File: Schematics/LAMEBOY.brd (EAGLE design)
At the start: 45.7 x 67.3 mm, 65 parts, among them IC1 PCF8574T, IC3 MCP73831, Q1 12MHz, U1 USD-SOCKETMICROSDEBAY, U2 USB

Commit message: labelstuff
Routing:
- net VCC: track 261.0 -> 260.4 mm
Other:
- board text added: "This will come in handy one day"
- board text removed: "This will come in handy one day. Please help."
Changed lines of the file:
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@@
 <wire x1="29.21" y1="28.448" x2="29.21" y2="14.732" width="0.254" layer="25"/>
 <wire x1="29.21" y1="14.732" x2="45.339" y2="14.732" width="0.254" layer="25"/>
-<text x="38.608" y="28.702" size="1.778" layer="25" ratio="12">SD</text>
+<text x="41.402" y="28.702" size="1.778" layer="25" ratio="12" rot="R90">SD</text>
 <text x="0.508" y="56.642" size="1.778" layer="26" ratio="15" rot="MR90">RST</text>
 <text x="45.085" y="58.039" size="1.778" layer="26" ratio="15" rot="MR0">C</text>
@@
 serial
 converter</text>
-<text x="38.1" y="21.59" size="1.016" layer="25" ratio="12" distance="5" rot="R180" align="center">This will come in
-handy one day.
-Please help.</text>
+<text x="38.1" y="21.59" size="1.016" layer="25" ratio="12" distance="5" rot="R180" align="center">This will come
+in handy
+one day</text>
 </plain>
 <attributes>
@@
 <contactref element="S2" pad="1"/>
 <wire x1="40.005" y1="52.07" x2="40.767" y2="51.308" width="0.4064" layer="1"/>
-<wire x1="40.767" y1="51.308" x2="40.767" y2="31.75" width="0.4064" layer="1"/>
-<wire x1="26.86091875" y1="31.2592" x2="40.2762" y2="31.2592" width="0.4064" layer="16"/>
-<wire x1="40.2762" y1="31.2592" x2="40.767" y2="31.75" width="0.4064" layer="16"/>
-<via x="40.767" y="31.75" extent="1-16" drill="0.3302" diameter="1.016"/>
+<wire x1="40.767" y1="51.308" x2="40.767" y2="32.512" width="0.4064" layer="1"/>
+<wire x1="26.86091875" y1="31.2592" x2="39.5142" y2="31.2592" width="0.4064" layer="16"/>
+<wire x1="39.5142" y1="31.2592" x2="40.767" y2="32.512" width="0.4064" layer="16"/>
+<via x="40.767" y="32.512" extent="1-16" drill="0.3302" diameter="1.016"/>
 <wire x1="21.86091875" y1="31.2592" x2="21.86091875" y2="34.90808125" width="0.4064" layer="16"/>
 <wire x1="21.86091875" y1="34.90808125" x2="21.844" y2="35.052" width="0.4064" layer="16"/>
@@
 <contactref element="C3" pad="P$1"/>
 <wire x1="34.326" y1="63.782" x2="34.326" y2="62.194" width="0.254" layer="1"/>
-<wire x1="40.64" y1="31.623" x2="40.767" y2="31.75" width="0.4064" layer="1"/>
 <contactref element="U$10" pad="P$2"/>
 <wire x1="2.286" y1="25.13" x2="2.27" y2="25.146" width="0.4064" layer="1"/>

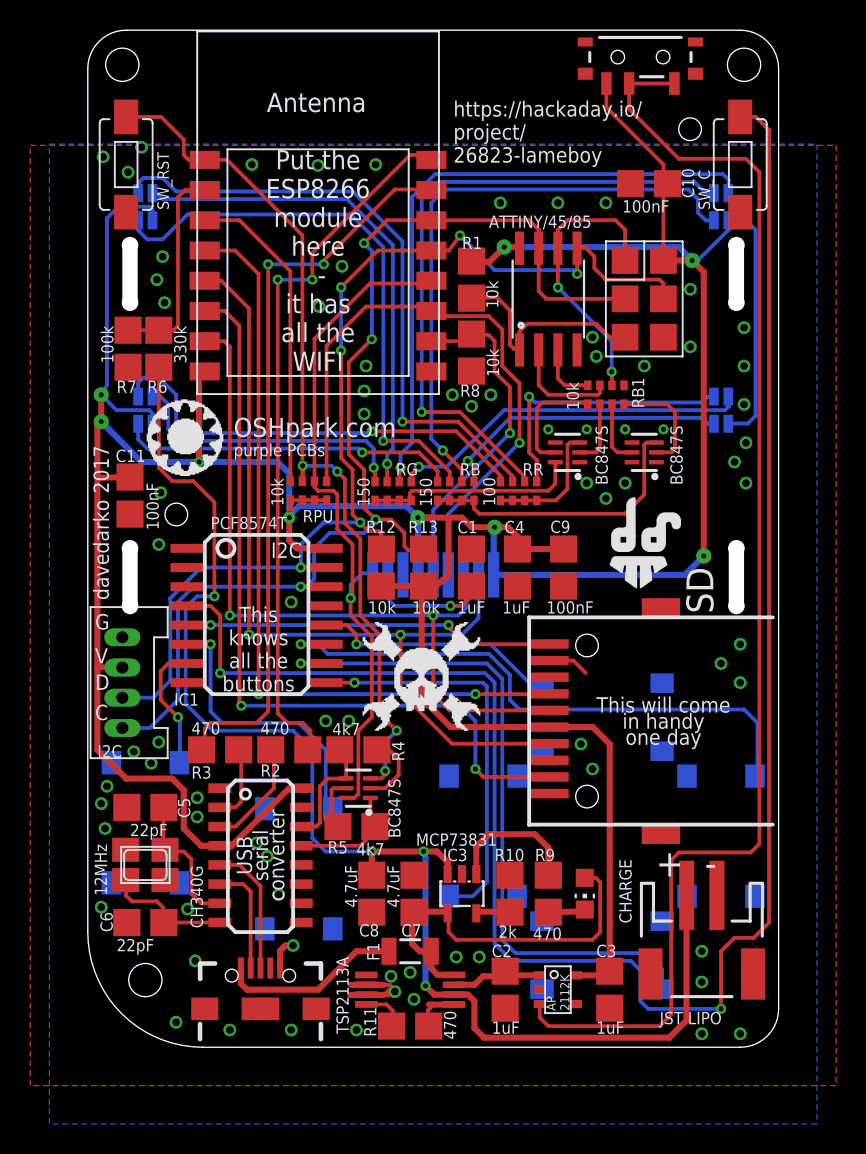
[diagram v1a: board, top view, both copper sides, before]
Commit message: moved C and RST switch
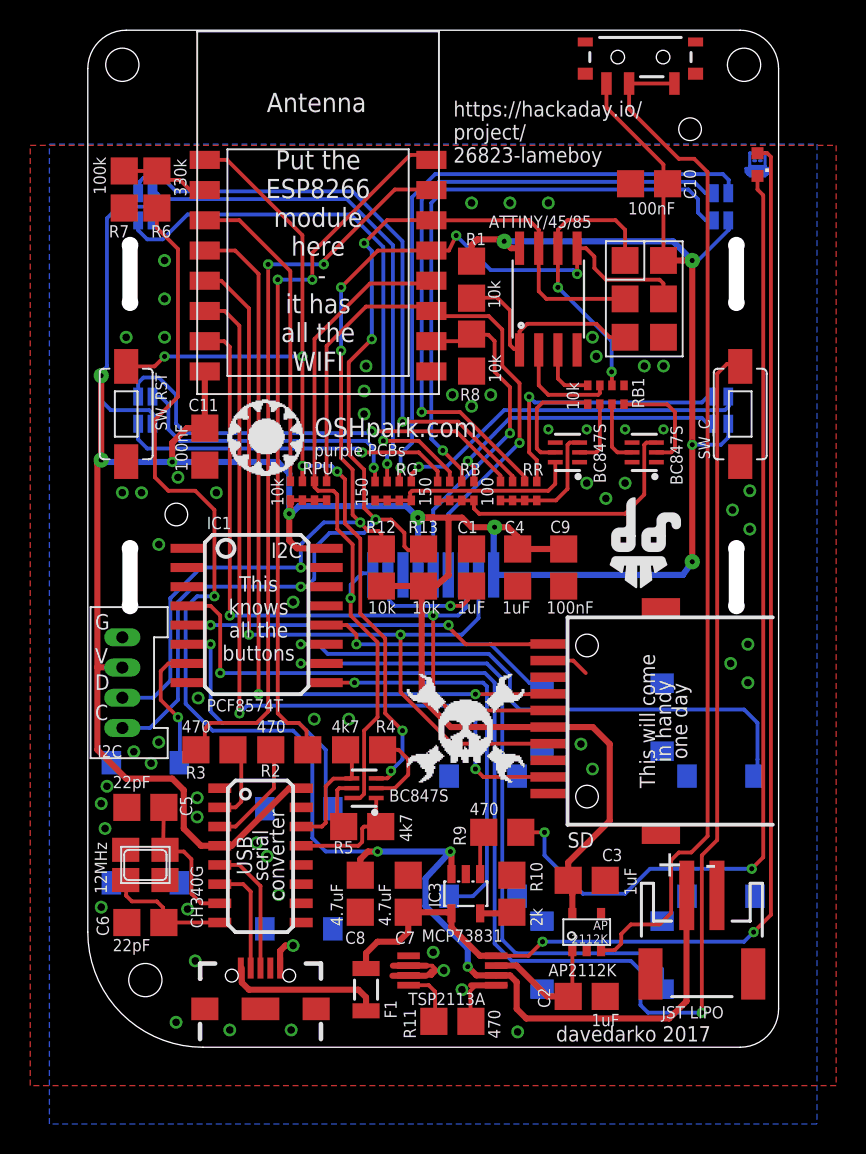
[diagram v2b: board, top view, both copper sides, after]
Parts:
- removed U$8: (no value), LOGOS:DAVEDARKO_GOLD
- added U$13: (no value), LOGOS:DAVEDARKO_GOLD
- CHARGE: device led:CHIP-LED0805 -> led:CHIPLED_0603_CHARLIE
- moved CHARGE 49.6 mm to (44.3, 58.4)
- moved SW_C 16.5 mm to (43.2, 41.9)
- moved SW_RST 16.5 mm to (2.54, 41.9)
- moved R7 10.5 mm to (2.41, 56.8)
- moved R6 10.5 mm to (4.57, 56.8)
- moved C3 7.40 mm to (33.0, 11.0), turned to 0 degrees
- moved C11 5.92 mm to (7.75, 39.8)
- moved C2 5.42 mm to (33.0, 3.37), turned to 0 degrees
- moved U$5 5.33 mm to (20.7, 40.4)
- moved R9 5.08 mm to (27.4, 14.2), turned to 180 degrees
- moved U$12 4.50 mm to (25.0, 20.8)
- moved U$9 4.26 mm to (33.0, 7.62), turned to 180 degrees
- moved F1 3.87 mm to (18.4, 3.81), turned to 90 degrees
- moved U$4 3.07 mm to (24.1, 5.08)
- moved R11 2.81 mm to (24.1, 1.71)
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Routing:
- net N$15: track 2.47 -> 64.9 mm, vias 0 -> 2
- net VBUS: track 24.9 -> 83.7 mm, vias 0 -> 2
- net BTN_C: track 122.4 -> 103.5 mm
- net VCC: track 260.4 -> 242.3 mm, vias 9 -> 10
- net VREG_EN: track 86.1 -> 68.2 mm
- net VBAT: track 94.4 -> 103.4 mm
- net ADC: track 14.4 -> 5.85 mm
- net N$12: track 9.11 -> 2.82 mm
- net N$16: track 0.00 -> 5.33 mm
- net RST_ESP: track 58.4 -> 63.5 mm, vias 4 -> 6
- net N$1: track 0.00 -> 3.81 mm
- net N$14: track 0.00 -> 2.03 mm
- net VREG_IN: track 6.76 -> 8.75 mm
- net N$20: track 3.17 -> 4.73 mm
- net VUSB: track 12.0 -> 10.5 mm
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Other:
- board text added: "AP2112K"
- board text added: "USB"

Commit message: usb logo
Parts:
- moved U$13 0.13 mm to (34.0, 12.8)
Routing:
- net N$14: track 2.03 -> 8.08 mm
- net N$16: track 5.33 -> 0.00 mm
- net N$15: track 64.9 -> 65.7 mm
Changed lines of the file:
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@@
 <layer number="28" name="bValues" color="7" fill="1" visible="no" active="yes"/>
 <layer number="29" name="tStop" color="7" fill="3" visible="no" active="yes"/>
-<layer number="30" name="bStop" color="7" fill="6" visible="yes" active="yes"/>
+<layer number="30" name="bStop" color="7" fill="6" visible="no" active="yes"/>
 <layer number="31" name="tCream" color="7" fill="4" visible="no" active="yes"/>
 <layer number="32" name="bCream" color="7" fill="5" visible="no" active="yes"/>
@@
 <element name="U$11" library="LOGOS" package="DAVEDARKO2_LOGO" value="" x="36.449" y="32.639"/>
 <element name="U$12" library="LOGOS" package="HACKADAY_LOGO" value="" x="24.9555" y="20.7645"/>
-<element name="U$13" library="LOGOS" package="DAVEDARKO_GOLD" value="" x="34.036" y="12.954" rot="MR0"/>
+<element name="U$13" library="LOGOS" package="DAVEDARKO_GOLD" value="" x="34.036" y="12.827" rot="MR0"/>
 </elements>
 <signals>
@@
 <via x="43.942" y="11.811" extent="1-16" drill="0.3302"/>
 <wire x1="28.657" y1="14.224" x2="30.226" y2="14.224" width="0.254" layer="1"/>
-<wire x1="30.226" y1="14.224" x2="30.226" y2="12.7" width="0.254" layer="16"/>
-<wire x1="30.226" y1="12.7" x2="32.766" y2="10.16" width="0.254" layer="16"/>
-<wire x1="32.766" y1="10.16" x2="35.56" y2="10.16" width="0.254" layer="16"/>
-<wire x1="35.56" y1="10.16" x2="37.211" y2="11.811" width="0.254" layer="16"/>
-<wire x1="37.211" y1="11.811" x2="43.942" y2="11.811" width="0.254" layer="16"/>
+<wire x1="30.226" y1="14.224" x2="30.226" y2="11.43" width="0.254" layer="16"/>
+<wire x1="30.226" y1="11.43" x2="31.75" y2="10.033" width="0.254" layer="16"/>
+<wire x1="31.75" y1="10.033" x2="35.56" y2="10.033" width="0.254" layer="16"/>
+<wire x1="35.56" y1="10.033" x2="37.338" y2="11.811" width="0.254" layer="16"/>
+<wire x1="37.338" y1="11.811" x2="43.942" y2="11.811" width="0.254" layer="16"/>
 <via x="30.226" y="14.224" extent="1-16" drill="0.3302"/>
 </signal>
@@
 </signal>
 <signal name="N$1">
-<wire x1="43.815" y1="59.182" x2="44.831" y2="59.182" width="0.2032" layer="16"/>
-<wire x1="44.831" y1="59.182" x2="44.831" y2="58.293" width="0.2032" layer="16"/>
+<wire x1="43.942" y1="59.182" x2="44.704" y2="59.182" width="0.2032" layer="16"/>
+<wire x1="44.704" y1="59.182" x2="44.831" y2="59.055" width="0.2032" layer="16"/>
+<wire x1="44.831" y1="59.055" x2="44.831" y2="58.293" width="0.2032" layer="16"/>
 <wire x1="44.831" y1="58.293" x2="43.815" y2="58.293" width="0.2032" layer="16"/>
-<wire x1="43.815" y1="58.293" x2="43.815" y2="59.182" width="0.2032" layer="16"/>
+<wire x1="43.815" y1="58.293" x2="43.815" y2="59.055" width="0.2032" layer="16"/>
+<wire x1="43.815" y1="59.055" x2="43.942" y2="59.182" width="0.2032" layer="16"/>
 </signal>
 <signal name="N$2">
@@
 <wire x1="43.561" y1="58.166" x2="45.085" y2="58.166" width="0.2032" layer="16"/>
 <wire x1="45.085" y1="58.166" x2="45.085" y2="57.912" width="0.2032" layer="16"/>
-</signal>
-<signal name="N$16">
 <wire x1="43.688" y1="58.039" x2="44.958" y2="58.039" width="0.2032" layer="16"/>
 <wire x1="44.958" y1="58.039" x2="44.958" y2="57.785" width="0.2032" layer="16"/>
@@
 <wire x1="43.688" y1="57.912" x2="44.831" y2="57.912" width="0.2032" layer="16"/>
 <wire x1="44.831" y1="57.912" x2="44.831" y2="57.658" width="0.1524" layer="16"/>
-<wire x1="44.831" y1="57.658" x2="43.815" y2="57.658" width="0.2032" layer="16"/>
+<wire x1="43.561" y1="57.912" x2="43.815" y2="57.658" width="0.2032" layer="16"/>
+<wire x1="43.815" y1="57.658" x2="44.831" y2="57.658" width="0.2032" layer="16"/>
+<wire x1="44.831" y1="57.658" x2="45.085" y2="57.912" width="0.2032" layer="16"/>
 </signal>
 </signals>

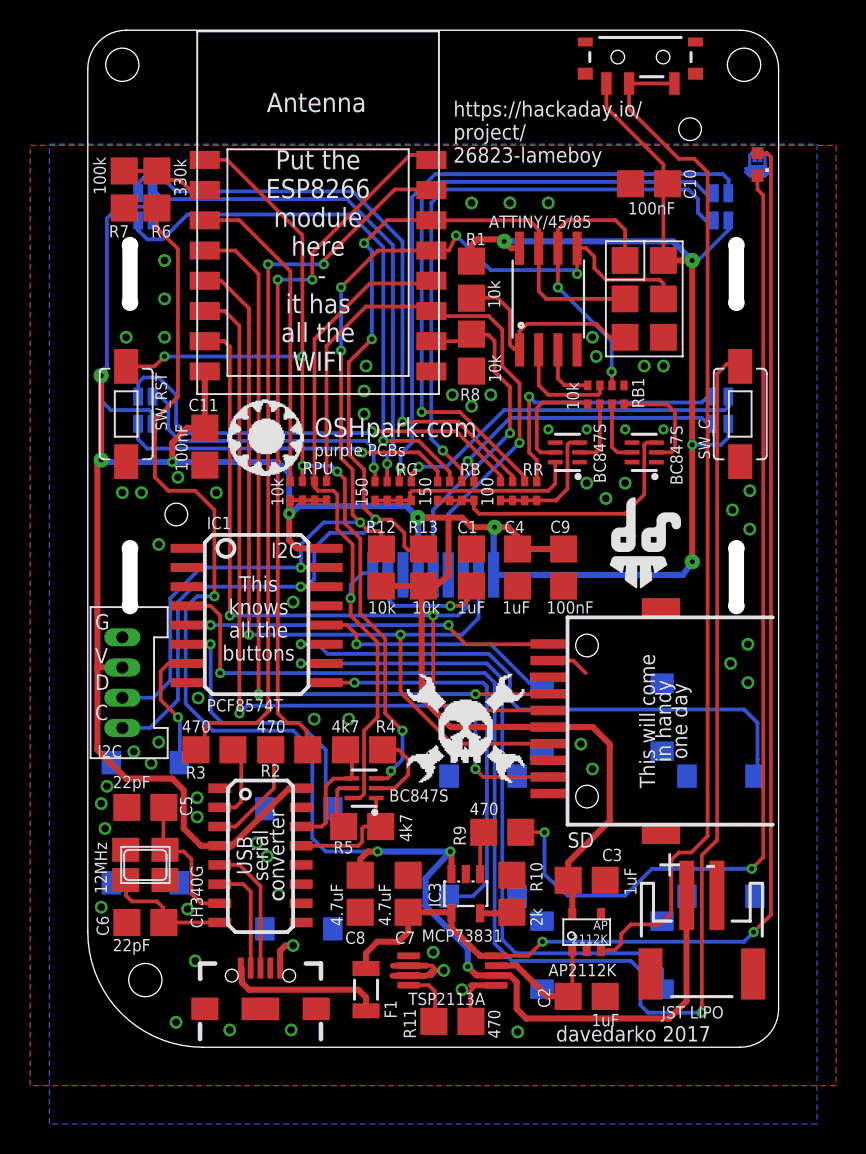
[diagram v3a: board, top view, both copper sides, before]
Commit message: wrong power for enabling regulator
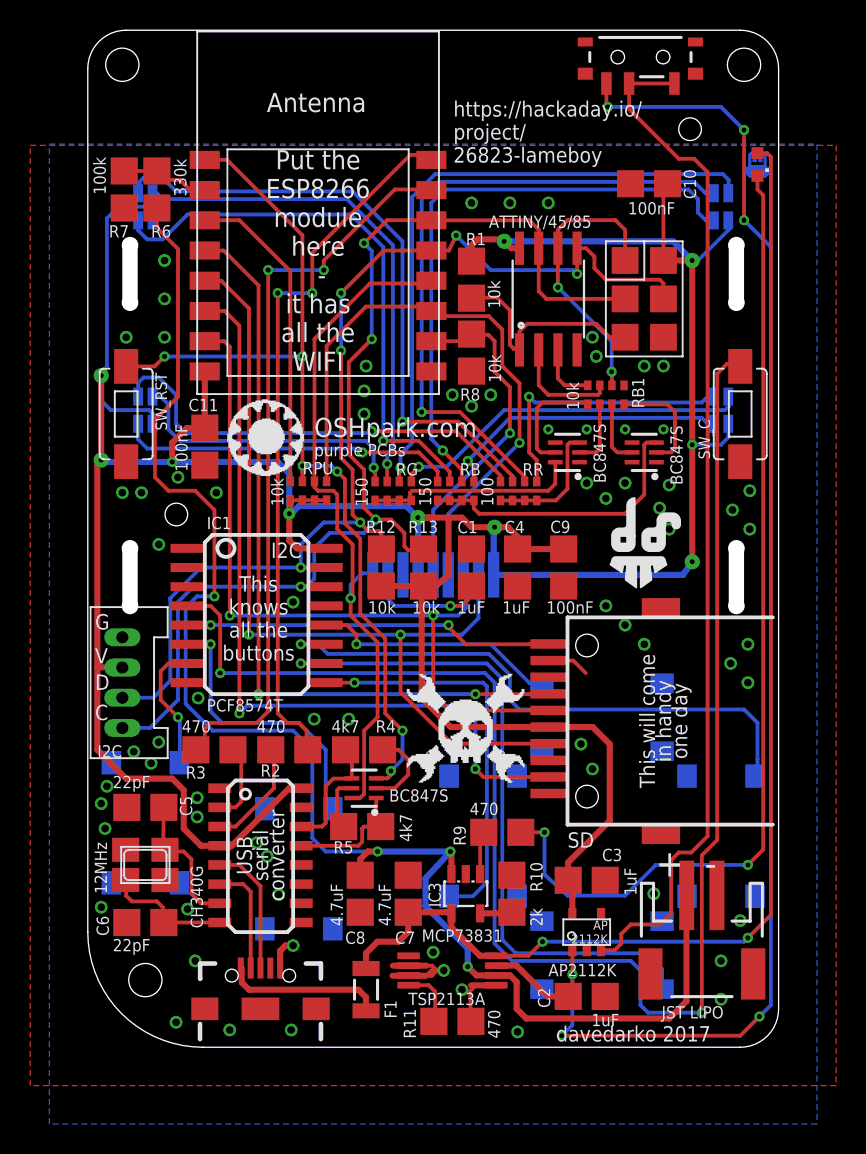
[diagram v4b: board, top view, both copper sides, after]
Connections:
- net VCC: no longer S2.1
- net VREG_IN: now also S2.1
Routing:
- net VREG_IN: track 8.75 -> 97.8 mm, vias 0 -> 6
- net VCC: track 242.3 -> 234.1 mm
- net GND: vias 63 -> 73
